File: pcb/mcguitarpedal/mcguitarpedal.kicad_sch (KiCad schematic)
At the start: 69 parts, among them J1 IN, J10 ENCODER2, J11 ENCODER3, J2 PREAMP_HEADERS, J3 BTN_MTX, J4 OUT, J5 EXP, J6 ILI9488 Module, J7 PWR_IN, J8 POT_HP_VOLUME_10k, J9 ENCODER1, Q1 Q_NPN_BCE, Q2 Q_PNP_BCE, SW1 SW_BYPASS, SW2 SW_TUNER, SW3 SW_PRESET, SW5 SW_PWR, U1 Teensy4.1, U2 Teensy Audio Board, U4 74HC148, U6 STPDWN-3P-5V, U7 STDN-3A24-ADJ, U8 74HCT595D

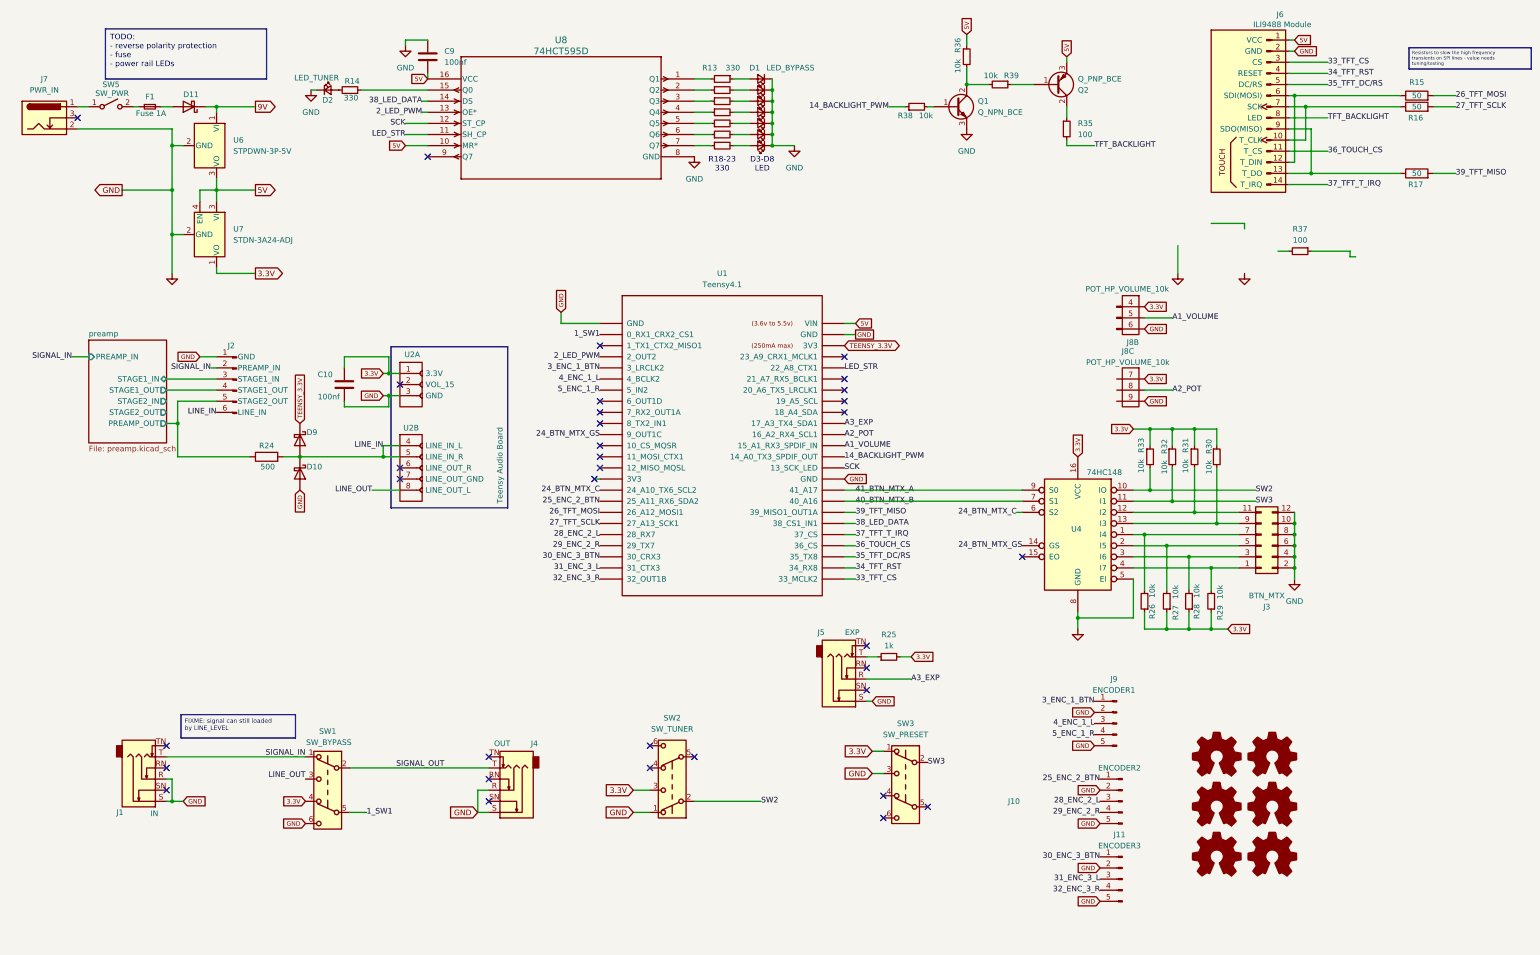
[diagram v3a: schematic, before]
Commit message: Backlight control, PWR leds
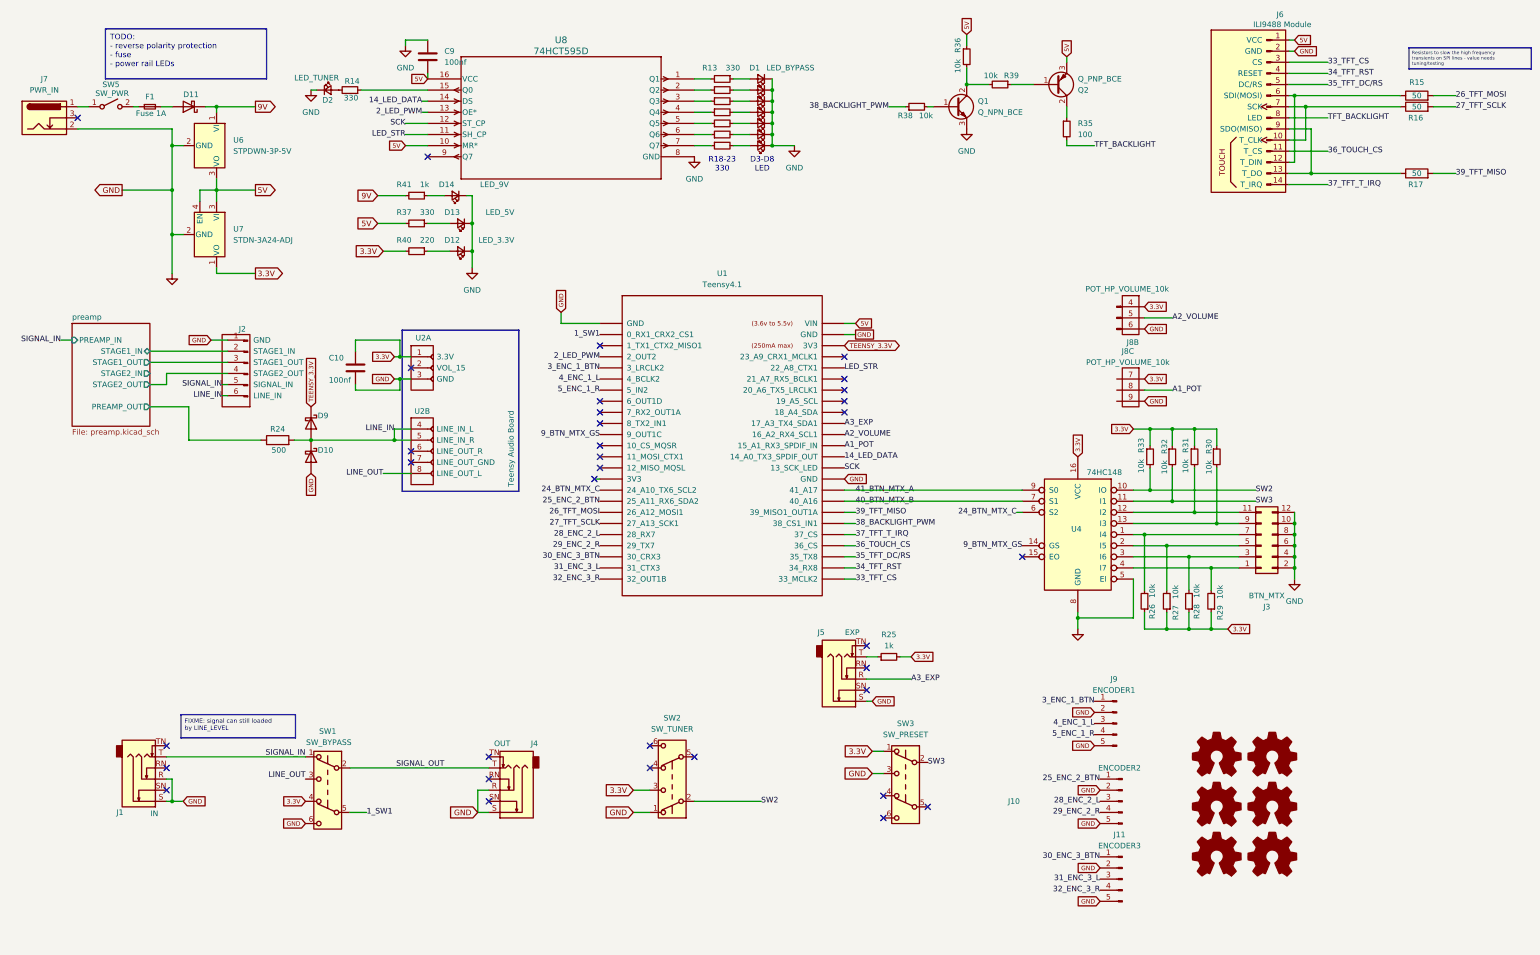
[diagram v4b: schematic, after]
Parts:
- added D12: LED_3.3V, mcguitarpedal:LED_D3.0mm, symbol Device:LED_Small
- added D13: LED_5V, mcguitarpedal:LED_D3.0mm, symbol Device:LED_Small
- added D14: LED_9V, mcguitarpedal:LED_D3.0mm, symbol Device:LED_Small
- added R40: 220, Resistor_SMD:R_1206_3216Metric_Pad1.30x1.75mm_HandSolder, symbol Device:R_Small
- added R41: 1k, Resistor_SMD:R_1206_3216Metric_Pad1.30x1.75mm_HandSolder, symbol Device:R_Small
- D10, D11, D9: footprint TI_FOOTPRINTS:DO-41_DIO -> Diode_THT:D_DO-41_SOD81_P10.16mm_Horizontal
- D8: value LED -> LED_STATUS; footprint mcguitarpedal:LED_D3.0mm -> LED_THT:LED_D5.0mm
- J2: symbol Connector:Conn_01x04_Pin -> mcguitarpedal:Preamp_headers
- Q1, Q2: footprint (none) -> Package_TO_SOT_THT:TO-92_Inline
- R37: value 100 -> 330; footprint Resistor_THT:R_Axial_DIN0207_L6.3mm_D2.5mm_P7.62mm_Horizontal -> Resistor_SMD:R_1206_3216Metric_Pad1.30x1.75mm_HandSolder
- U1: footprint mcguitarpedal:Teensy 4.1 with audio board -> mcguitarpedal:Teensy 4.1
- U7: footprint Connector_PinSocket_2.54mm:PinSocket_1x04_P2.54mm_Vertical -> mcguitarpedal:STPDN-3A24-ADJ
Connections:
- net 3.3V: now also R40.2
- net 5V: now also R37.2
- net 9V: now also R41.2
- net GND: now also D12.1 (K), D13.1 (K), D14.1 (K)
- net SIGNAL_IN: now also J2.5 (SIGNAL_IN); no longer J2.2 (PREAMP_IN)
- net preamp/PREAMP_OUT: no longer J2.5 (STAGE2_OUT)
- net preamp/STAGE1_IN: now also J2.2 (STAGE1_IN); no longer J2.3 (STAGE1_IN)
- net preamp/STAGE1_OUT: now also J2.3 (STAGE1_OUT); no longer J2.4 (STAGE1_OUT)
- net preamp/STAGE2_OUT: now also J2.4 (STAGE2_OUT)
- net at R37.1: now also D13.2 (A)
- net 14_BACKLIGHT_PWM renamed 14_LED_DATA
- net 14_LED_DATA: now also U8.14 (DS); no longer R38.1
- net 24_BTN_MTX_GS renamed 9_BTN_MTX_GS
- net 38_LED_DATA renamed 38_BACKLIGHT_PWM
- net 38_BACKLIGHT_PWM: now also R38.1; no longer U8.14 (DS)
- net A1_VOLUME renamed A1_POT
- net A1_POT: now also J8.8 (Pin_8); no longer J8.5 (Pin_5)
- net A2_POT renamed A2_VOLUME
- net A2_VOLUME: now also J8.5 (Pin_5); no longer J8.8 (Pin_8)
- new net: D12.2 (A), R40.1
- new net: D14.2 (A), R41.1
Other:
- moved on the sheet: C10, D10, D9, R24, U2A, U2B
